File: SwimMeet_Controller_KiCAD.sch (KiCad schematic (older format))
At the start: 35 parts, among them SW1 KEY, SW10 KEY, SW11 KEY, SW12 KEY, SW13 KEY, SW2 KEY, SW3 KEY, SW4 KEY, SW5 KEY, SW6 KEY, SW7 KEY, SW8 KEY, SW9 KEY, U1 Digispark_USB-A_16.5MHz, U2 MCP23017-E_SO

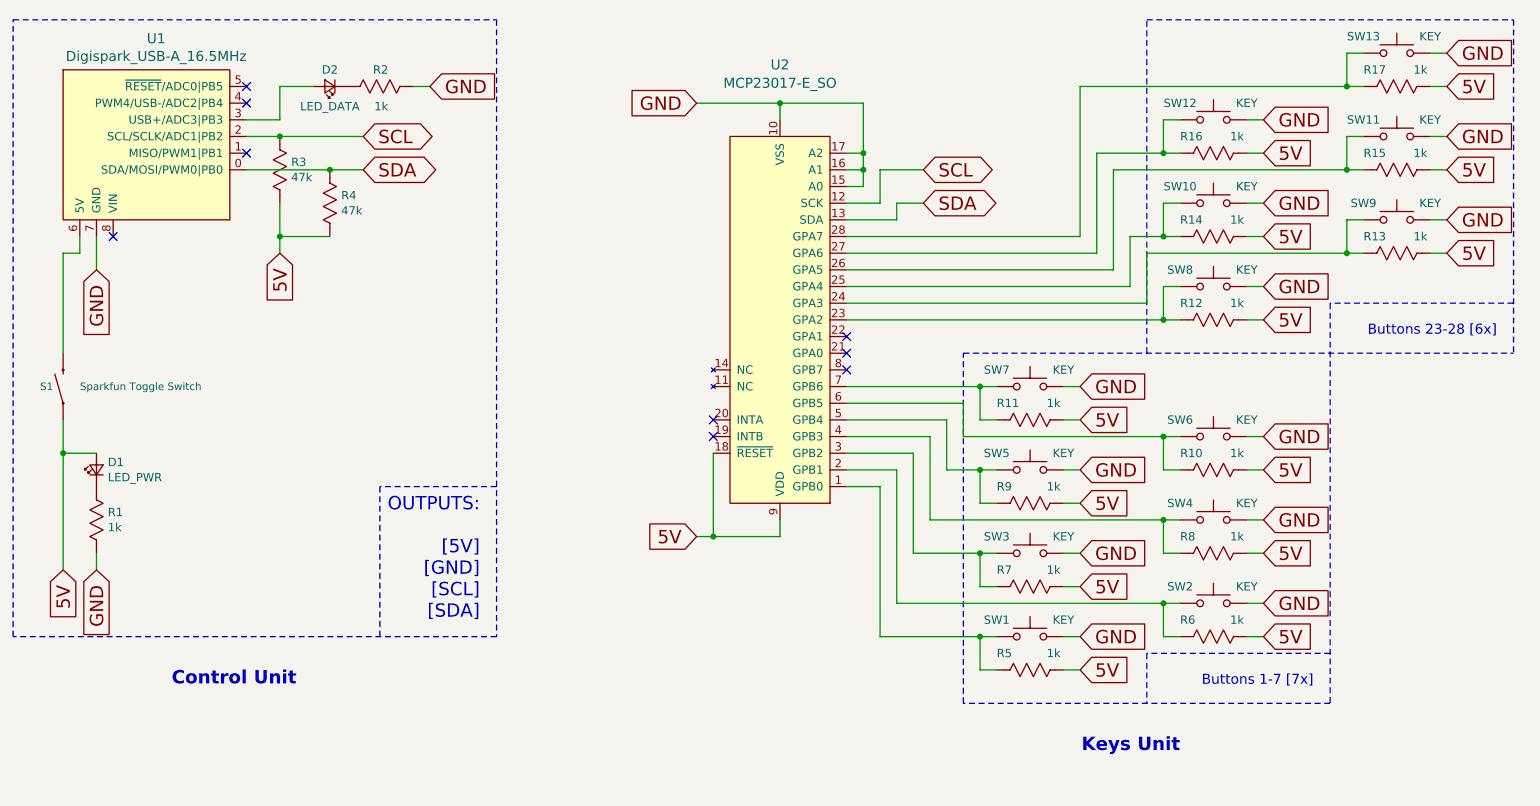
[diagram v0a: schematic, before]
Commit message: used proper power symbols in schem; made schem compatible with larger grid size; added net names; tidy'ed up PCB more
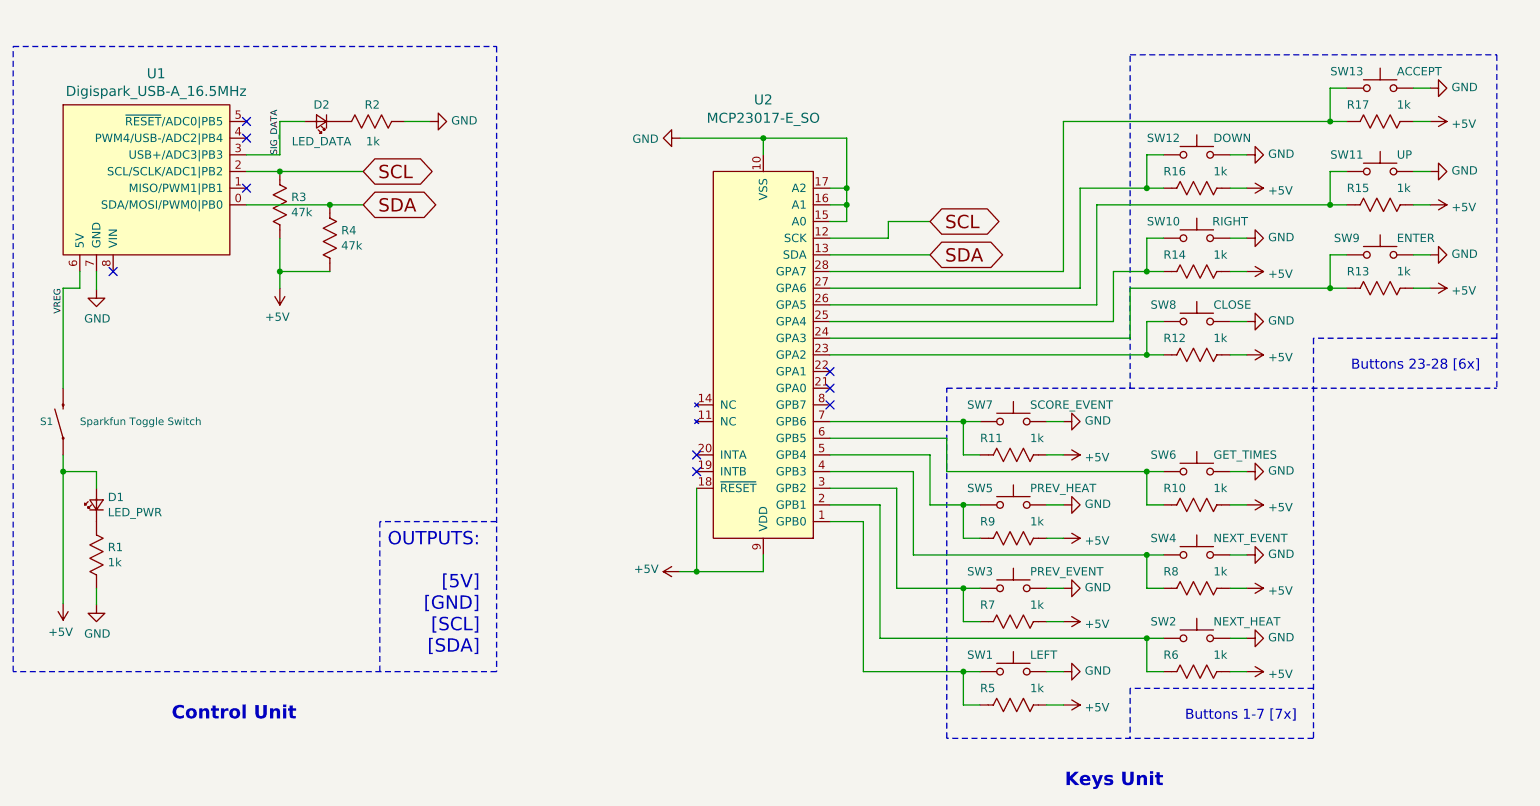
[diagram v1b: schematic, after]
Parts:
- SW1: value KEY -> LEFT
- SW10: value KEY -> RIGHT
- SW11: value KEY -> UP
- SW12: value KEY -> DOWN
- SW13: value KEY -> ACCEPT
- SW2: value KEY -> NEXT_HEAT
- SW3: value KEY -> PREV_EVENT
- SW4: value KEY -> NEXT_EVENT
- SW5: value KEY -> PREV_HEAT
- SW6: value KEY -> GET_TIMES
- SW7: value KEY -> SCORE_EVENT
- SW8: value KEY -> CLOSE
- SW9: value KEY -> ENTER
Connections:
- net SIG_DATA: now reaches D2.2 (A), U1.3 (USB+/ADC3|PB3)
- net VREG: now reaches S1.2, U1.6 (5V)
- net 5V renamed +5V
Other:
- moved on the sheet: D1, D2, R1, R10, R11, R12, R13, R14, R15, R16, R17, R2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

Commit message: implemented polygons for 5V+ net
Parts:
- R1: value 1k -> 150R
- R2: value 1k -> 100R
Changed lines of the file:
@@
 Sheet 1 1
 Title "Swim Meet Commander"
-Date "2019-12-27"
-Rev "2019-12-27"
+Date "2019-12-30"
+Rev "2019-12-30"
 Comp "Samm Du"
 Comment1 "https://sammdu.com"
@@
 P 3150 1900
 F 0 "R2" V 3250 1850 50  0000 L CNN
-F 1 "1k" V 3030 1850 50  0000 L CNN
+F 1 "100R" V 3025 1800 50  0000 L CNN
 F 2 "Resistor_SMD:R_0805_2012Metric_Pad1.15x1.40mm_HandSolder" V 3080 1900 50  0001 C CNN
 F 3 "~" H 3150 1900 50  0001 C CNN
@@
 P 2850 1900
 F 0 "D2" H 2850 1800 50  0000 C CNN
-F 1 "LED_DATA" H 2850 2020 50  0000 C CNN
+F 1 "LED_DATA" H 2850 2025 50  0000 C CNN
 F 2 "LED_THT:LED_D5.0mm" V 2850 1900 50  0001 C CNN
 F 3 "~" V 2850 1900 50  0001 C CNN
@@
 P 1500 4500
 F 0 "R1" H 1568 4546 50  0000 L CNN
-F 1 "1k" H 1568 4455 50  0000 L CNN
+F 1 "150R" H 1568 4455 50  0000 L CNN
 F 2 "Resistor_SMD:R_0805_2012Metric_Pad1.15x1.40mm_HandSolder" V 1430 4500 50  0001 C CNN
 F 3 "~" H 1500 4500 50  0001 C CNN

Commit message: adjusted resistor values, updated F.Silk graphic, updated toggle switch footprint
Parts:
- R1: value 150R -> 330R
- R10, R11, R12, R13, R14, R15, R16, R17, R5, R6, R7, R8, R9: value 1k -> 10k
- R2: value 100R -> 330R
- R3, R4: value 47k -> 4k7
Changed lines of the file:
@@
 Sheet 1 1
 Title "Swim Meet Commander"
-Date "2019-12-31"
-Rev "2019-12-31"
+Date "2020-01-08"
+Rev "2020-01-08"
 Comp "Samm Du"
 Comment1 "https://github.com/sammdu/SwimMeet_Commander"
@@
 P 2600 2400
 F 0 "R3" H 2668 2446 50  0000 L CNN
-F 1 "47k" H 2668 2355 50  0000 L CNN
+F 1 "4k7" H 2668 2355 50  0000 L CNN
 F 2 "Resistor_SMD:R_0805_2012Metric_Pad1.15x1.40mm_HandSolder" V 2530 2400 50  0001 C CNN
 F 3 "~" H 2600 2400 50  0001 C CNN
@@
 P 2900 2600
 F 0 "R4" H 2968 2646 50  0000 L CNN
-F 1 "47k" H 2968 2555 50  0000 L CNN
+F 1 "4k7" H 2968 2555 50  0000 L CNN
 F 2 "Resistor_SMD:R_0805_2012Metric_Pad1.15x1.40mm_HandSolder" V 2830 2600 50  0001 C CNN
 F 3 "~" H 2900 2600 50  0001 C CNN
@@
 P 3150 1900
 F 0 "R2" V 3250 1850 50  0000 L CNN
-F 1 "100R" V 3025 1800 50  0000 L CNN
+F 1 "330R" V 3025 1800 50  0000 L CNN
 F 2 "Resistor_SMD:R_0805_2012Metric_Pad1.15x1.40mm_HandSolder" V 3080 1900 50  0001 C CNN
 F 3 "~" H 3150 1900 50  0001 C CNN
@@
 P 7000 3900
 F 0 "R11" V 6900 3700 50  0000 L CNN
-F 1 "1k" V 6900 4000 50  0000 L CNN
+F 1 "10k" V 6900 4000 50  0000 L CNN
 F 2 "Resistor_SMD:R_0805_2012Metric_Pad1.15x1.40mm_HandSolder" V 6930 3900 50  0001 C CNN
 F 3 "~" H 7000 3900 50  0001 C CNN
@@
 P 7000 4400
 F 0 "R9" V 6900 4200 50  0000 L CNN
-F 1 "1k" V 6900 4500 50  0000 L CNN
+F 1 "10k" V 6900 4500 50  0000 L CNN
 F 2 "Resistor_SMD:R_0805_2012Metric_Pad1.15x1.40mm_HandSolder" V 6930 4400 50  0001 C CNN
 F 3 "~" H 7000 4400 50  0001 C CNN
@@
 P 7000 4900
 F 0 "R7" V 6900 4700 50  0000 L CNN
-F 1 "1k" V 6900 5000 50  0000 L CNN
+F 1 "10k" V 6900 5000 50  0000 L CNN
 F 2 "Resistor_SMD:R_0805_2012Metric_Pad1.15x1.40mm_HandSolder" V 6930 4900 50  0001 C CNN
 F 3 "~" H 7000 4900 50  0001 C CNN
@@
 P 7000 5400
 F 0 "R5" V 6900 5200 50  0000 L CNN
-F 1 "1k" V 6900 5500 50  0000 L CNN
+F 1 "10k" V 6900 5500 50  0000 L CNN
 F 2 "Resistor_SMD:R_0805_2012Metric_Pad1.15x1.40mm_HandSolder" V 6930 5400 50  0001 C CNN
 F 3 "~" H 7000 5400 50  0001 C CNN
@@
 P 8100 4200
 F 0 "R10" V 8000 4000 50  0000 L CNN
-F 1 "1k" V 8000 4300 50  0000 L CNN
+F 1 "10k" V 8000 4300 50  0000 L CNN
 F 2 "Resistor_SMD:R_0805_2012Metric_Pad1.15x1.40mm_HandSolder" V 8030 4200 50  0001 C CNN
 F 3 "~" H 8100 4200 50  0001 C CNN
@@
 P 8100 4700
 F 0 "R8" V 8000 4500 50  0000 L CNN
-F 1 "1k" V 8000 4800 50  0000 L CNN
+F 1 "10k" V 8000 4800 50  0000 L CNN
 F 2 "Resistor_SMD:R_0805_2012Metric_Pad1.15x1.40mm_HandSolder" V 8030 4700 50  0001 C CNN
 F 3 "~" H 8100 4700 50  0001 C CNN
@@
 P 8100 5200
 F 0 "R6" V 8000 5000 50  0000 L CNN
-F 1 "1k" V 8000 5300 50  0000 L CNN
+F 1 "10k" V 8000 5300 50  0000 L CNN
 F 2 "Resistor_SMD:R_0805_2012Metric_Pad1.15x1.40mm_HandSolder" V 8030 5200 50  0001 C CNN
 F 3 "~" H 8100 5200 50  0001 C CNN
@@
 P 8100 2300
 F 0 "R16" V 8000 2100 50  0000 L CNN
-F 1 "1k" V 8000 2400 50  0000 L CNN
+F 1 "10k" V 8000 2400 50  0000 L CNN
 F 2 "Resistor_SMD:R_0805_2012Metric_Pad1.15x1.40mm_HandSolder" V 8030 2300 50  0001 C CNN
 F 3 "~" H 8100 2300 50  0001 C CNN
@@
 P 8100 2800
 F 0 "R14" V 8000 2600 50  0000 L CNN
-F 1 "1k" V 8000 2900 50  0000 L CNN
+F 1 "10k" V 8000 2900 50  0000 L CNN
 F 2 "Resistor_SMD:R_0805_2012Metric_Pad1.15x1.40mm_HandSolder" V 8030 2800 50  0001 C CNN
 F 3 "~" H 8100 2800 50  0001 C CNN
@@
 P 8100 3300
 F 0 "R12" V 8000 3100 50  0000 L CNN
-F 1 "1k" V 8000 3400 50  0000 L CNN
+F 1 "10k" V 8000 3400 50  0000 L CNN
 F 2 "Resistor_SMD:R_0805_2012Metric_Pad1.15x1.40mm_HandSolder" V 8030 3300 50  0001 C CNN
 F 3 "~" H 8100 3300 50  0001 C CNN
@@
 P 9200 1900
 F 0 "R17" V 9100 1700 50  0000 L CNN
-F 1 "1k" V 9100 2000 50  0000 L CNN
+F 1 "10k" V 9100 2000 50  0000 L CNN
 F 2 "Resistor_SMD:R_0805_2012Metric_Pad1.15x1.40mm_HandSolder" V 9130 1900 50  0001 C CNN
 F 3 "~" H 9200 1900 50  0001 C CNN
@@
 P 9200 2400
 F 0 "R15" V 9100 2200 50  0000 L CNN
-F 1 "1k" V 9100 2500 50  0000 L CNN
+F 1 "10k" V 9100 2500 50  0000 L CNN
 F 2 "Resistor_SMD:R_0805_2012Metric_Pad1.15x1.40mm_HandSolder" V 9130 2400 50  0001 C CNN
 F 3 "~" H 9200 2400 50  0001 C CNN
@@
 P 9200 2900
 F 0 "R13" V 9100 2700 50  0000 L CNN
-F 1 "1k" V 9100 3000 50  0000 L CNN
+F 1 "10k" V 9100 3000 50  0000 L CNN
 F 2 "Resistor_SMD:R_0805_2012Metric_Pad1.15x1.40mm_HandSolder" V 9130 2900 50  0001 C CNN
 F 3 "~" H 9200 2900 50  0001 C CNN
@@
 P 1500 4500
 F 0 "R1" H 1568 4546 50  0000 L CNN
-F 1 "150R" H 1568 4455 50  0000 L CNN
+F 1 "330R" H 1568 4455 50  0000 L CNN
 F 2 "Resistor_SMD:R_0805_2012Metric_Pad1.15x1.40mm_HandSolder" V 1430 4500 50  0001 C CNN
 F 3 "~" H 1500 4500 50  0001 C CNN

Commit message: MAJOR REVISION 2020-01-12
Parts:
- added R4: 10k, Resistor_SMD:R_0805_2012Metric_Pad1.15x1.40mm_HandSolder, symbol SAMM_Misc:R_US
- added S2: DEBUG, spk_Switches:SWITCH_SPST_SMD_A, symbol SparkFun-Switches:SWITCH-SPDT-SMD-RIGHT-ANGLE
- renumbered R9 to R10, R10 to R11, R11 to R12, R12 to R13, R13 to R14, R14 to R15, R15 to R16, R16 to R17, R17 to R18, R4 to R5, R5 to R6, R6 to R7, R7 to R8, R8 to R9
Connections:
- net +5V: now also S2.3 (S)
- net GND: now also R4.2
- net SIG_DEBUG: now reaches U1.1 (MISO/PWM1|PB1)
- net SIG_DEBUG: now also R4.1, S2.2 (P)
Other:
- moved on the sheet: D1, D2, R1, R10, R11, R12, R13, R14, R15, R16, R17, R18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
